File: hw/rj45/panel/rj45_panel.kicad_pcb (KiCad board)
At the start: 6 copper layers, 71.4 x 107 mm, 471 parts, among them J1 SFP edge (INF-8074i), J2 KH-RJ45-58-8P8C, T1 LP72450ANL, U1 RTL8221B-VB-CG, U2 STM32G031F6P6, U3 TPS62822DLC, U4 TPS22918DBVR, X1 MST8011AI-72-33E25

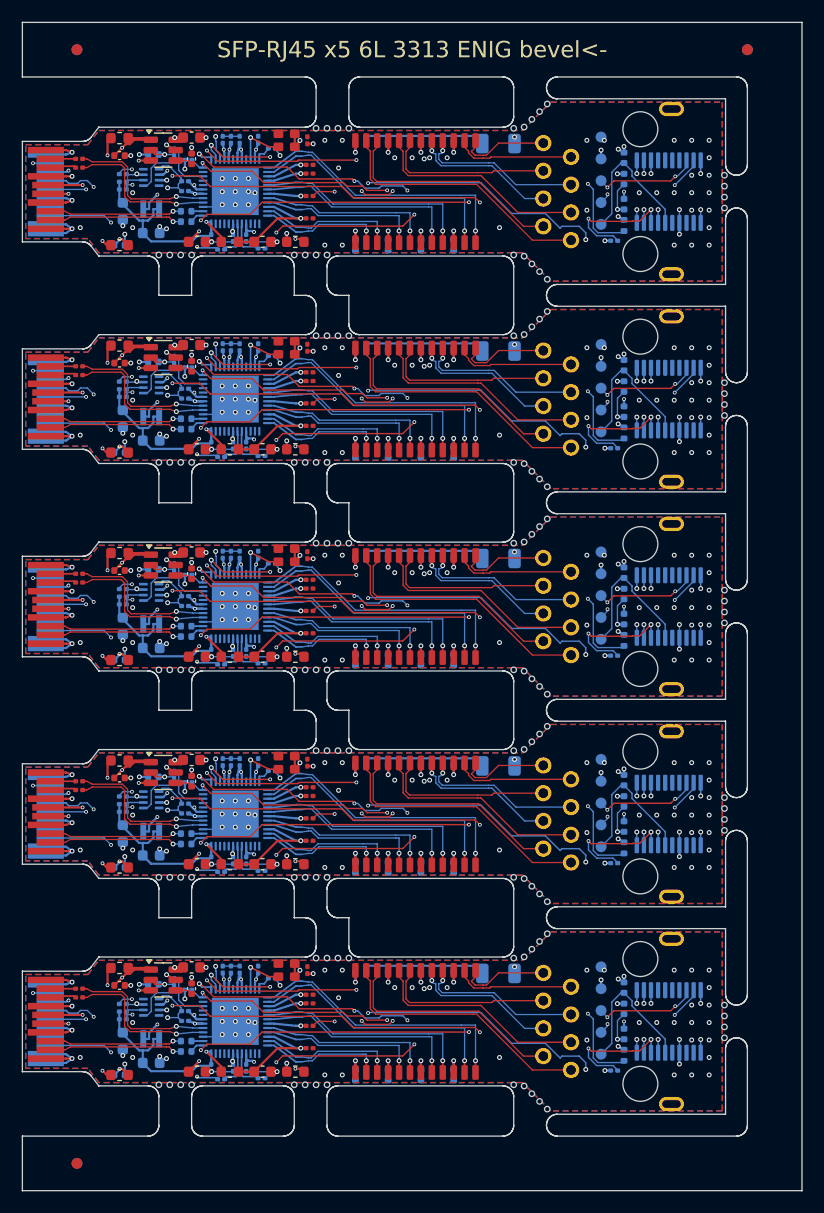
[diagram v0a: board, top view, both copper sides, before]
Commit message: RJ45 re-laid on the corrected SFP edge: U1 on top
With the edge drawn the right way round (SFF-8419 Figure 7-2) the RTL8221B's
SerDes pins meet RD-, RD+, TD+, TD- straight only from the top side; it has
no SerDes polarity swap. U1's group (decaps, straps, fan, oscillator, analog
beads, HSO caps) is turned over as one body in make_rj45.py; the links to
the rest are laid new:
- HSI and RD pairs on top, P to P, no via
- MDI on top under the magnetics' body straight into the chip-side pads,
  port 0 on channel 1; CFG_OPT1 now pulled down (no MDI swap)
- the slow lines laid on In2 end to end in the jack bus's lane order; the
  MCU's GPIOs follow it (fw VARIANT_RJ45: PA0 MDIO, PA1 MDC, PA4 TX_FAULT,
  PA5 TX_DISABLE, PA6 RX_LOS)
- both VCC beads, the load switch and its caps below the HSI pair; the
  buck's switch node under its own body; panel tabs moved off U4 and X1
DRC 0 / 0 unconnected, ERC 0, KiCad 9 PASS, panel 0 errors. T1S still
carries the mirrored edge.
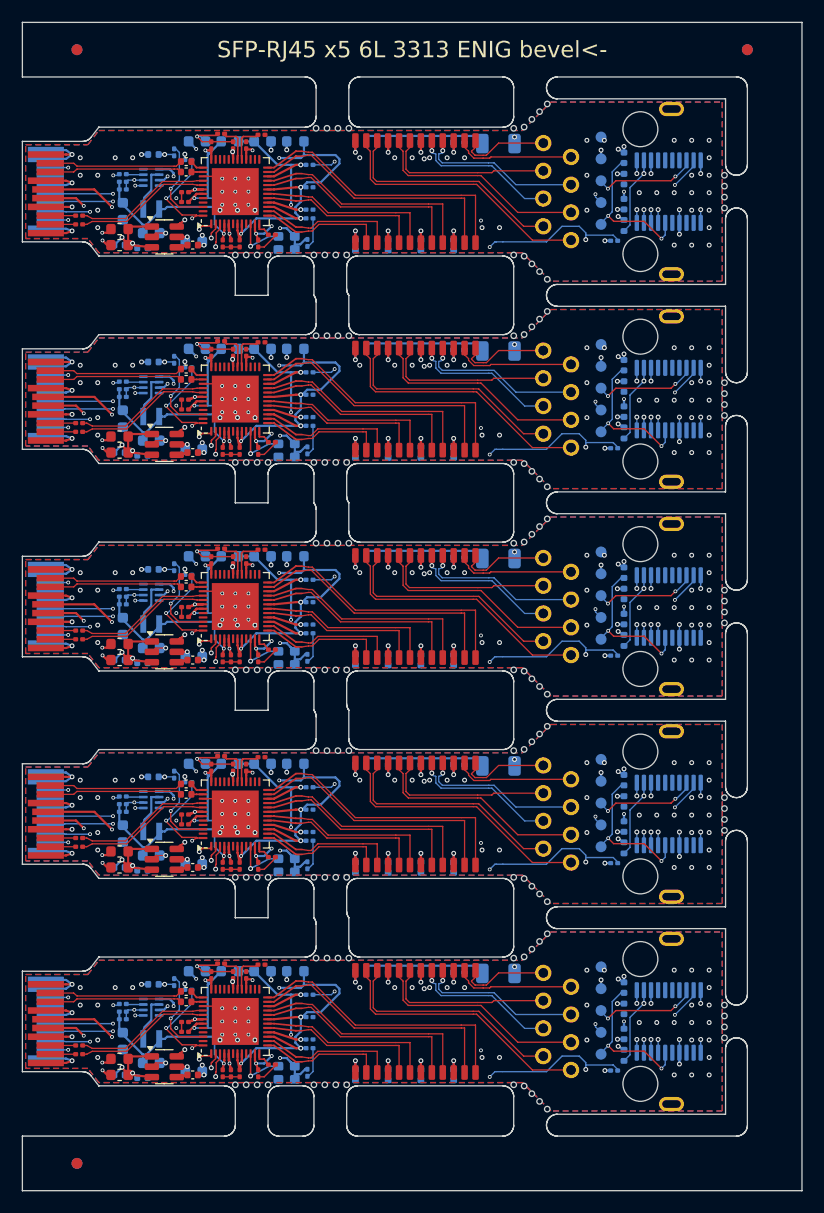
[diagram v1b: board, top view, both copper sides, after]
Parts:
- removed the C1 at (121.7, 89.2)
- removed the C1 at (121.7, 70.2)
- removed the C1 at (121.7, 51.2)
- removed the C1 at (121.7, 108.2)
- removed the C1 at (121.7, 32.2)
- removed the C10 at (134.4, 49.8)
- removed the C10 at (134.4, 87.8)
- removed the C10 at (134.4, 30.8)
- removed the C10 at (134.4, 106.8)
- removed the C10 at (134.4, 68.8)
- removed the C11 at (139.1, 109.0)
- removed the C11 at (139.1, 71.0)
- removed the C11 at (139.1, 33.0)
- removed the C11 at (139.1, 90.0)
- removed the C11 at (139.1, 52.0)
- removed the C12 at (139.1, 33.9)
- removed the C12 at (139.1, 52.9)
- removed the C12 at (139.1, 71.8)
- removed the C12 at (139.1, 90.8)
- removed the C12 at (139.1, 109.8)
- removed the C13 at (139.1, 73.9)
- removed the C13 at (139.1, 35.9)
- removed the C13 at (139.1, 54.9)
- removed the C13 at (139.1, 92.9)
- removed the C13 at (139.1, 111.9)
- removed the C14 at (139.1, 57.0)
- removed the C14 at (139.1, 95.0)
- removed the C14 at (139.1, 38.0)
- removed the C14 at (139.1, 114.0)
- removed the C14 at (139.1, 76.0)
- removed the C15 at (133.3, 77.8)
- removed the C15 at (133.3, 96.8)
- removed the C15 at (133.3, 58.8)
- removed the C15 at (133.3, 39.8)
- removed the C15 at (133.3, 115.8)
- removed the C16 at (132.1, 58.8)
- removed the C16 at (132.1, 115.8)
- removed the C16 at (132.1, 96.8)
- removed the C16 at (132.1, 39.8)
- removed the C16 at (132.1, 77.8)
- removed the C17 at (130.1, 77.8)
- removed the C17 at (130.1, 39.8)
- removed the C17 at (130.1, 58.8)
- removed the C17 at (130.1, 115.8)
- removed the C17 at (130.1, 96.8)
- removed the C18 at (127.7, 92.5)
- removed the C18 at (127.7, 73.5)
- removed the C18 at (127.7, 111.5)
- removed the C18 at (127.7, 35.5)
- removed the C18 at (127.7, 54.5)
- removed the C19 at (127.7, 34.5)
- removed the C19 at (127.7, 110.5)
- removed the C19 at (127.7, 53.5)
- removed the C19 at (127.7, 72.5)
- removed the C19 at (127.7, 91.5)
- removed the C21 at (134.8, 59.1)
- removed the C21 at (134.8, 116.1)
- removed the C21 at (134.8, 97.1)
- removed the C21 at (134.8, 78.1)
- removed the C21 at (134.8, 40.1)
- removed the C22 at (128.8, 40.1)
- removed the C22 at (128.8, 78.1)
- removed the C22 at (128.8, 97.1)
- removed the C22 at (128.8, 59.1)
- removed the C22 at (128.8, 116.1)
- removed the C3 at (118.0, 90.3)
- removed the C3 at (118.0, 33.3)
- removed the C3 at (118.0, 109.3)
- removed the C3 at (118.0, 71.3)
- removed the C3 at (118.0, 52.3)
- removed the C30 at (138.9, 106.8)
- removed the C30 at (138.9, 30.8)
- removed the C30 at (138.9, 68.8)
- removed the C30 at (138.9, 87.8)
- removed the C30 at (138.9, 49.8)
- removed the C4 at (118.0, 108.5)
- removed the C4 at (118.0, 70.5)
- removed the C4 at (118.0, 51.5)
- removed the C4 at (118.0, 89.5)
- removed the C4 at (118.0, 32.5)
- removed the C44 at (128.3, 89.5)
- removed the C44 at (128.3, 32.5)
- removed the C44 at (128.3, 108.5)
- removed the C44 at (128.3, 70.5)
- removed the C44 at (128.3, 51.5)
- removed the C45 at (128.3, 68.5)
- removed the C45 at (128.3, 87.5)
- removed the C45 at (128.3, 49.5)
- removed the C45 at (128.3, 106.5)
- removed the C45 at (128.3, 30.6)
- removed the C5 at (127.8, 56.3)
- removed the C5 at (127.8, 94.3)
- removed the C5 at (127.8, 37.3)
- removed the C5 at (127.8, 113.3)
- removed the C5 at (127.8, 75.3)
- removed the C6 at (127.8, 114.2)
- removed the C6 at (127.8, 38.2)
- removed the C6 at (127.8, 95.2)
- removed the C6 at (127.8, 76.2)
- removed the C6 at (127.8, 57.2)
- removed the C7 at (131.2, 106.8)
- removed the C7 at (131.2, 49.8)
- removed the C7 at (131.2, 30.8)
- removed the C7 at (131.2, 68.8)
- removed the C7 at (131.2, 87.8)
- removed the C8 at (131.9, 30.8)
- removed the C8 at (131.9, 106.8)
- removed the C8 at (131.9, 87.8)
- removed the C8 at (131.9, 68.8)
- removed the C8 at (131.9, 49.8)
- removed the C9 at (132.7, 87.8)
- removed the C9 at (132.7, 106.8)
- removed the C9 at (132.7, 68.8)
- removed the C9 at (132.7, 49.8)
- removed the C9 at (132.7, 30.8)
- removed the FB1 at (121.7, 49.6)
- removed the FB1 at (121.7, 87.6)
- removed the FB1 at (121.7, 30.6)
- removed the FB1 at (121.7, 68.6)
- removed the FB1 at (121.7, 106.6)
- removed the FB2 at (121.7, 78.4)
- removed the FB2 at (121.7, 116.4)
- removed the FB2 at (121.7, 40.4)
- removed the FB2 at (121.7, 59.4)
- removed the FB2 at (121.7, 97.4)
- removed the FB3 at (131.8, 97.1)
- removed the FB3 at (131.8, 116.1)
- removed the FB3 at (131.8, 59.1)
- removed the FB3 at (131.8, 40.1)
- removed the FB3 at (131.8, 78.1)
- removed the FB4 at (137.8, 116.1)
- removed the FB4 at (137.8, 97.1)
- removed the FB4 at (137.8, 78.1)
- removed the FB4 at (137.8, 40.1)
- removed the FB4 at (137.8, 59.1)
- removed KiKit_MB_12_5, KiKit_MB_18_5, KiKit_MB_24_5, KiKit_MB_30_5, KiKit_MB_6_5: NPTH, NPTH
- removed the R12 at (134.7, 116.7)
- removed the R12 at (134.7, 78.7)
- removed the R12 at (134.7, 40.7)
- removed the R12 at (134.7, 97.7)
- removed the R12 at (134.7, 59.7)
- removed the R13 at (131.0, 116.8)
- removed the R13 at (131.0, 59.8)
- removed the R13 at (131.0, 40.8)
- removed the R13 at (131.0, 78.8)
- removed the R13 at (131.0, 97.8)
- removed the R9 at (135.7, 88.5)
- removed the R9 at (135.7, 31.6)
- removed the R9 at (135.7, 107.5)
- removed the R9 at (135.7, 69.5)
- removed the R9 at (135.7, 50.5)
- removed the U4 at (125.7, 69.7)
- removed the U4 at (125.7, 50.7)
- removed the U4 at (125.7, 107.7)
- removed the U4 at (125.7, 88.7)
- removed the U4 at (125.7, 31.7)
- removed the X1 at (137.0, 30.8)
- removed the X1 at (137.0, 68.8)
- removed the X1 at (137.0, 106.8)
- removed the X1 at (137.0, 49.8)
- removed the X1 at (137.0, 87.8)
- added C1: 1uF, Capacitor_SMD:C_0402_1005Metric, B.Cu at (123.8, 116.7)
- added C1: 1uF, Capacitor_SMD:C_0402_1005Metric, B.Cu at (123.8, 78.7)
- added C1: 1uF, Capacitor_SMD:C_0402_1005Metric, B.Cu at (123.8, 97.7)
- added C1: 1uF, Capacitor_SMD:C_0402_1005Metric, B.Cu at (123.8, 59.6)
- added C1: 1uF, Capacitor_SMD:C_0402_1005Metric, B.Cu at (123.8, 40.6)
- added C10: 100nF, Capacitor_SMD:C_0201_0603Metric, F.Cu at (134.4, 59.2)
- added C10: 100nF, Capacitor_SMD:C_0201_0603Metric, F.Cu at (134.4, 116.2)
- added C10: 100nF, Capacitor_SMD:C_0201_0603Metric, F.Cu at (134.4, 40.2)
- added C10: 100nF, Capacitor_SMD:C_0201_0603Metric, F.Cu at (134.4, 97.2)
- added C10: 100nF, Capacitor_SMD:C_0201_0603Metric, F.Cu at (134.4, 78.2)
- added C11: 100nF, Capacitor_SMD:C_0201_0603Metric, B.Cu at (139.1, 57.0)
- added C11: 100nF, Capacitor_SMD:C_0201_0603Metric, B.Cu at (139.1, 38.0)
- added C11: 100nF, Capacitor_SMD:C_0201_0603Metric, B.Cu at (139.1, 95.0)
- added C11: 100nF, Capacitor_SMD:C_0201_0603Metric, B.Cu at (139.1, 114.0)
- added C11: 100nF, Capacitor_SMD:C_0201_0603Metric, B.Cu at (139.1, 76.0)
- added C12: 100nF, Capacitor_SMD:C_0201_0603Metric, B.Cu at (139.1, 56.1)
- added C12: 100nF, Capacitor_SMD:C_0201_0603Metric, B.Cu at (139.1, 94.2)
- added C12: 100nF, Capacitor_SMD:C_0201_0603Metric, B.Cu at (139.1, 37.1)
- added C12: 100nF, Capacitor_SMD:C_0201_0603Metric, B.Cu at (139.1, 113.2)
- added C12: 100nF, Capacitor_SMD:C_0201_0603Metric, B.Cu at (139.1, 75.2)
- added C13: 100nF, Capacitor_SMD:C_0201_0603Metric, B.Cu at (139.1, 35.1)
- added C13: 100nF, Capacitor_SMD:C_0201_0603Metric, B.Cu at (139.1, 111.1)
- added C13: 100nF, Capacitor_SMD:C_0201_0603Metric, B.Cu at (139.1, 73.1)
- added C13: 100nF, Capacitor_SMD:C_0201_0603Metric, B.Cu at (139.1, 54.1)
- added C13: 100nF, Capacitor_SMD:C_0201_0603Metric, B.Cu at (139.1, 92.1)
- added C14: 100nF, Capacitor_SMD:C_0201_0603Metric, B.Cu at (139.1, 52.0)
- added C14: 100nF, Capacitor_SMD:C_0201_0603Metric, B.Cu at (139.1, 90.0)
- added C14: 100nF, Capacitor_SMD:C_0201_0603Metric, B.Cu at (139.1, 33.0)
- added C14: 100nF, Capacitor_SMD:C_0201_0603Metric, B.Cu at (139.1, 109.0)
- added C14: 100nF, Capacitor_SMD:C_0201_0603Metric, B.Cu at (139.1, 71.0)
- added C15: 100nF, Capacitor_SMD:C_0201_0603Metric, F.Cu at (133.3, 107.2)
- added C15: 100nF, Capacitor_SMD:C_0201_0603Metric, F.Cu at (133.3, 50.2)
- added C15: 100nF, Capacitor_SMD:C_0201_0603Metric, F.Cu at (133.3, 31.2)
- added C15: 100nF, Capacitor_SMD:C_0201_0603Metric, F.Cu at (133.3, 69.2)
- added C15: 100nF, Capacitor_SMD:C_0201_0603Metric, F.Cu at (133.3, 88.2)
- added C16: 100nF, Capacitor_SMD:C_0201_0603Metric, F.Cu at (132.1, 88.2)
- added C16: 100nF, Capacitor_SMD:C_0201_0603Metric, F.Cu at (132.1, 50.2)
- added C16: 100nF, Capacitor_SMD:C_0201_0603Metric, F.Cu at (132.1, 107.2)
- added C16: 100nF, Capacitor_SMD:C_0201_0603Metric, F.Cu at (132.1, 69.2)
- added C16: 100nF, Capacitor_SMD:C_0201_0603Metric, F.Cu at (132.1, 31.2)
- added C17: 100nF, Capacitor_SMD:C_0201_0603Metric, F.Cu at (130.1, 88.2)
- added C17: 100nF, Capacitor_SMD:C_0201_0603Metric, F.Cu at (130.1, 69.2)
- added C17: 100nF, Capacitor_SMD:C_0201_0603Metric, F.Cu at (130.1, 50.2)
- added C17: 100nF, Capacitor_SMD:C_0201_0603Metric, F.Cu at (130.1, 107.2)
- added C17: 100nF, Capacitor_SMD:C_0201_0603Metric, F.Cu at (130.1, 31.2)
- added C18: 100nF, Capacitor_SMD:C_0201_0603Metric, F.Cu at (127.7, 111.5)
- added C18: 100nF, Capacitor_SMD:C_0201_0603Metric, F.Cu at (127.7, 92.5)
- added C18: 100nF, Capacitor_SMD:C_0201_0603Metric, F.Cu at (127.7, 73.5)
- added C18: 100nF, Capacitor_SMD:C_0201_0603Metric, F.Cu at (127.7, 35.5)
- added C18: 100nF, Capacitor_SMD:C_0201_0603Metric, F.Cu at (127.7, 54.5)
- added C19: 100nF, Capacitor_SMD:C_0201_0603Metric, F.Cu at (127.7, 93.5)
- added C19: 100nF, Capacitor_SMD:C_0201_0603Metric, F.Cu at (127.7, 74.5)
- added C19: 100nF, Capacitor_SMD:C_0201_0603Metric, F.Cu at (127.7, 36.5)
- added C19: 100nF, Capacitor_SMD:C_0201_0603Metric, F.Cu at (127.7, 112.5)
- added C19: 100nF, Capacitor_SMD:C_0201_0603Metric, F.Cu at (127.7, 55.5)
- added C21: 10uF, Capacitor_SMD:C_0603_1608Metric, B.Cu at (134.8, 106.9)
- added C21: 10uF, Capacitor_SMD:C_0603_1608Metric, B.Cu at (134.8, 68.9)
- added C21: 10uF, Capacitor_SMD:C_0603_1608Metric, B.Cu at (134.8, 49.9)
- added C21: 10uF, Capacitor_SMD:C_0603_1608Metric, B.Cu at (134.8, 30.9)
- added C21: 10uF, Capacitor_SMD:C_0603_1608Metric, B.Cu at (134.8, 87.9)
- added C22: 10uF, Capacitor_SMD:C_0603_1608Metric, B.Cu at (128.8, 106.9)
- added C22: 10uF, Capacitor_SMD:C_0603_1608Metric, B.Cu at (128.8, 68.9)
- added C22: 10uF, Capacitor_SMD:C_0603_1608Metric, B.Cu at (128.8, 49.9)
- added C22: 10uF, Capacitor_SMD:C_0603_1608Metric, B.Cu at (128.8, 87.9)
- added C22: 10uF, Capacitor_SMD:C_0603_1608Metric, B.Cu at (128.8, 30.9)
- added C3: 100nF, Capacitor_SMD:C_0201_0603Metric, F.Cu at (118.0, 75.7)
- added C3: 100nF, Capacitor_SMD:C_0201_0603Metric, F.Cu at (118.0, 56.7)
- added C3: 100nF, Capacitor_SMD:C_0201_0603Metric, F.Cu at (118.0, 37.7)
- added C3: 100nF, Capacitor_SMD:C_0201_0603Metric, F.Cu at (118.0, 113.7)
- added C3: 100nF, Capacitor_SMD:C_0201_0603Metric, F.Cu at (118.0, 94.7)
- added C30: 100nF, Capacitor_SMD:C_0201_0603Metric, B.Cu at (138.9, 78.2)
- added C30: 100nF, Capacitor_SMD:C_0201_0603Metric, B.Cu at (138.9, 116.2)
- added C30: 100nF, Capacitor_SMD:C_0201_0603Metric, B.Cu at (138.9, 40.2)
- added C30: 100nF, Capacitor_SMD:C_0201_0603Metric, B.Cu at (138.9, 97.2)
- added C30: 100nF, Capacitor_SMD:C_0201_0603Metric, B.Cu at (138.9, 59.2)
- added C4: 100nF, Capacitor_SMD:C_0201_0603Metric, F.Cu at (118.0, 95.5)
- added C4: 100nF, Capacitor_SMD:C_0201_0603Metric, F.Cu at (118.0, 76.5)
- added C4: 100nF, Capacitor_SMD:C_0201_0603Metric, F.Cu at (118.0, 38.5)
- added C4: 100nF, Capacitor_SMD:C_0201_0603Metric, F.Cu at (118.0, 57.5)
- added C4: 100nF, Capacitor_SMD:C_0201_0603Metric, F.Cu at (118.0, 114.5)
- added C44: 2.2nF, Capacitor_SMD:C_0402_1005Metric, F.Cu at (128.4, 40.4)
- added C44: 2.2nF, Capacitor_SMD:C_0402_1005Metric, F.Cu at (128.4, 116.4)
- added C44: 2.2nF, Capacitor_SMD:C_0402_1005Metric, F.Cu at (128.4, 78.4)
- added C44: 2.2nF, Capacitor_SMD:C_0402_1005Metric, F.Cu at (128.4, 59.4)
- added C44: 2.2nF, Capacitor_SMD:C_0402_1005Metric, F.Cu at (128.4, 97.4)
- added C45: 10uF, Capacitor_SMD:C_0603_1608Metric, B.Cu at (128.5, 116.1)
- added C45: 10uF, Capacitor_SMD:C_0603_1608Metric, B.Cu at (128.5, 40.1)
- added C45: 10uF, Capacitor_SMD:C_0603_1608Metric, B.Cu at (128.5, 97.1)
- added C45: 10uF, Capacitor_SMD:C_0603_1608Metric, B.Cu at (128.5, 78.1)
- added C45: 10uF, Capacitor_SMD:C_0603_1608Metric, B.Cu at (128.5, 59.1)
- added C5: 100nF, Capacitor_SMD:C_0402_1005Metric, F.Cu at (127.8, 33.7)
- added C5: 100nF, Capacitor_SMD:C_0402_1005Metric, F.Cu at (127.8, 90.7)
- added C5: 100nF, Capacitor_SMD:C_0402_1005Metric, F.Cu at (127.8, 52.7)
- added C5: 100nF, Capacitor_SMD:C_0402_1005Metric, F.Cu at (127.8, 109.7)
- added C5: 100nF, Capacitor_SMD:C_0402_1005Metric, F.Cu at (127.8, 71.7)
- added C6: 100nF, Capacitor_SMD:C_0402_1005Metric, F.Cu at (127.8, 108.8)
- added C6: 100nF, Capacitor_SMD:C_0402_1005Metric, F.Cu at (127.8, 51.8)
- added C6: 100nF, Capacitor_SMD:C_0402_1005Metric, F.Cu at (127.8, 70.8)
- added C6: 100nF, Capacitor_SMD:C_0402_1005Metric, F.Cu at (127.8, 32.8)
- added C6: 100nF, Capacitor_SMD:C_0402_1005Metric, F.Cu at (127.8, 89.8)
- added C7: 100nF, Capacitor_SMD:C_0201_0603Metric, F.Cu at (131.2, 97.2)
- added C7: 100nF, Capacitor_SMD:C_0201_0603Metric, F.Cu at (131.2, 59.2)
- added C7: 100nF, Capacitor_SMD:C_0201_0603Metric, F.Cu at (131.2, 116.2)
- added C7: 100nF, Capacitor_SMD:C_0201_0603Metric, F.Cu at (131.2, 40.2)
- added C7: 100nF, Capacitor_SMD:C_0201_0603Metric, F.Cu at (131.2, 78.2)
- added C8: 100nF, Capacitor_SMD:C_0201_0603Metric, F.Cu at (131.9, 116.2)
- added C8: 100nF, Capacitor_SMD:C_0201_0603Metric, F.Cu at (131.9, 59.2)
- added C8: 100nF, Capacitor_SMD:C_0201_0603Metric, F.Cu at (131.9, 40.2)
- added C8: 100nF, Capacitor_SMD:C_0201_0603Metric, F.Cu at (131.9, 97.2)
- added C8: 100nF, Capacitor_SMD:C_0201_0603Metric, F.Cu at (131.9, 78.2)
- added C9: 100nF, Capacitor_SMD:C_0201_0603Metric, F.Cu at (132.7, 59.2)
- added C9: 100nF, Capacitor_SMD:C_0201_0603Metric, F.Cu at (132.7, 78.2)
- added C9: 100nF, Capacitor_SMD:C_0201_0603Metric, F.Cu at (132.7, 116.2)
- added C9: 100nF, Capacitor_SMD:C_0201_0603Metric, F.Cu at (132.7, 97.2)
- added C9: 100nF, Capacitor_SMD:C_0201_0603Metric, F.Cu at (132.7, 40.2)
- added FB1: BLM18KG601SH1, Inductor_SMD:L_0603_1608Metric, F.Cu at (121.7, 59.4)
- added FB1: BLM18KG601SH1, Inductor_SMD:L_0603_1608Metric, F.Cu at (121.7, 97.4)
- added FB1: BLM18KG601SH1, Inductor_SMD:L_0603_1608Metric, F.Cu at (121.7, 116.4)
- added FB1: BLM18KG601SH1, Inductor_SMD:L_0603_1608Metric, F.Cu at (121.7, 78.4)
- added FB1: BLM18KG601SH1, Inductor_SMD:L_0603_1608Metric, F.Cu at (121.7, 40.4)
- added FB2: BLM18KG601SH1, Inductor_SMD:L_0603_1608Metric, F.Cu at (121.7, 114.9)
- added FB2: BLM18KG601SH1, Inductor_SMD:L_0603_1608Metric, F.Cu at (121.7, 57.9)
- added FB2: BLM18KG601SH1, Inductor_SMD:L_0603_1608Metric, F.Cu at (121.7, 38.9)
- added FB2: BLM18KG601SH1, Inductor_SMD:L_0603_1608Metric, F.Cu at (121.7, 95.9)
- added FB2: BLM18KG601SH1, Inductor_SMD:L_0603_1608Metric, F.Cu at (121.7, 76.9)
- added FB3: BLM18KG601SH1, Inductor_SMD:L_0603_1608Metric, B.Cu at (131.8, 106.9)
- added FB3: BLM18KG601SH1, Inductor_SMD:L_0603_1608Metric, B.Cu at (131.8, 30.9)
- added FB3: BLM18KG601SH1, Inductor_SMD:L_0603_1608Metric, B.Cu at (131.8, 49.9)
- added FB3: BLM18KG601SH1, Inductor_SMD:L_0603_1608Metric, B.Cu at (131.8, 68.9)
- added FB3: BLM18KG601SH1, Inductor_SMD:L_0603_1608Metric, B.Cu at (131.8, 87.9)
- added FB4: BLM18KG601SH1, Inductor_SMD:L_0603_1608Metric, B.Cu at (137.8, 87.9)
- added FB4: BLM18KG601SH1, Inductor_SMD:L_0603_1608Metric, B.Cu at (137.8, 68.9)
- added FB4: BLM18KG601SH1, Inductor_SMD:L_0603_1608Metric, B.Cu at (137.8, 49.9)
- added FB4: BLM18KG601SH1, Inductor_SMD:L_0603_1608Metric, B.Cu at (137.8, 30.9)
- added FB4: BLM18KG601SH1, Inductor_SMD:L_0603_1608Metric, B.Cu at (137.8, 106.9)
- added KiKit_MB_10_5: NPTH, NPTH, F.Cu at (160.9, 46.5)
- added KiKit_MB_16_5: NPTH, NPTH, F.Cu at (160.9, 65.5)
- added KiKit_MB_22_5: NPTH, NPTH, F.Cu at (160.9, 84.5)
- added KiKit_MB_28_5: NPTH, NPTH, F.Cu at (160.9, 103.5)
- added KiKit_MB_4_5: NPTH, NPTH, F.Cu at (160.9, 27.5)
- added R12: 4.7k, Resistor_SMD:R_0201_0603Metric, F.Cu at (134.7, 30.3)
- added R12: 4.7k, Resistor_SMD:R_0201_0603Metric, F.Cu at (134.7, 106.3)
- added R12: 4.7k, Resistor_SMD:R_0201_0603Metric, F.Cu at (134.7, 87.3)
- added R12: 4.7k, Resistor_SMD:R_0201_0603Metric, F.Cu at (134.7, 68.3)
- added R12: 4.7k, Resistor_SMD:R_0201_0603Metric, F.Cu at (134.7, 49.3)
- added R13: 4.7k, Resistor_SMD:R_0201_0603Metric, F.Cu at (131.0, 30.2)
- added R13: 4.7k, Resistor_SMD:R_0201_0603Metric, F.Cu at (131.0, 87.2)
- added R13: 4.7k, Resistor_SMD:R_0201_0603Metric, F.Cu at (131.0, 49.2)
- added R13: 4.7k, Resistor_SMD:R_0201_0603Metric, F.Cu at (131.0, 68.2)
- added R13: 4.7k, Resistor_SMD:R_0201_0603Metric, F.Cu at (131.0, 106.2)
- added R9: 2.49k 1%, Resistor_SMD:R_0201_0603Metric, F.Cu at (135.7, 77.5)
- added R9: 2.49k 1%, Resistor_SMD:R_0201_0603Metric, F.Cu at (135.7, 58.5)
- added R9: 2.49k 1%, Resistor_SMD:R_0201_0603Metric, F.Cu at (135.7, 115.5)
- added R9: 2.49k 1%, Resistor_SMD:R_0201_0603Metric, F.Cu at (135.7, 39.5)
- added R9: 2.49k 1%, Resistor_SMD:R_0201_0603Metric, F.Cu at (135.7, 96.5)
- added U4: TPS22918DBVR, Package_TO_SOT_SMD:SOT-23-6, F.Cu at (125.8, 39.6)
- added U4: TPS22918DBVR, Package_TO_SOT_SMD:SOT-23-6, F.Cu at (125.8, 96.7)
- added U4: TPS22918DBVR, Package_TO_SOT_SMD:SOT-23-6, F.Cu at (125.8, 77.7)
- added U4: TPS22918DBVR, Package_TO_SOT_SMD:SOT-23-6, F.Cu at (125.8, 115.7)
- added U4: TPS22918DBVR, Package_TO_SOT_SMD:SOT-23-6, F.Cu at (125.8, 58.6)
- added X1: MST8011AI-72-33E25, sfp:Oscillator_SMD_MST_2016-4Pin, B.Cu at (137.0, 116.2)
- added X1: MST8011AI-72-33E25, sfp:Oscillator_SMD_MST_2016-4Pin, B.Cu at (137.0, 40.2)
- added X1: MST8011AI-72-33E25, sfp:Oscillator_SMD_MST_2016-4Pin, B.Cu at (137.0, 78.2)
- added X1: MST8011AI-72-33E25, sfp:Oscillator_SMD_MST_2016-4Pin, B.Cu at (137.0, 59.2)
- added X1: MST8011AI-72-33E25, sfp:Oscillator_SMD_MST_2016-4Pin, B.Cu at (137.0, 97.2)
- U1 (x5): moved to F.Cu
- moved KiKit_MB_13_4 52.0 mm to (177.1, 75.0)
- moved KiKit_MB_19_4 52.0 mm to (177.1, 94.0)
- moved KiKit_MB_1_4 52.0 mm to (177.1, 37.0)
- moved KiKit_MB_25_4 52.0 mm to (177.1, 113.0)
- moved KiKit_MB_7_4 52.0 mm to (177.1, 56.0)
- moved KiKit_MB_13_3 51.1 mm to (177.1, 74.0)
- moved KiKit_MB_19_3 51.1 mm to (177.1, 93.0)
- moved KiKit_MB_1_3 51.1 mm to (177.1, 36.0)
- moved KiKit_MB_25_3 51.1 mm to (177.1, 112.0)
- moved KiKit_MB_7_3 51.1 mm to (177.1, 55.0)
- moved KiKit_MB_13_2 50.2 mm to (177.1, 73.0)
- moved KiKit_MB_19_2 50.2 mm to (177.1, 92.0)
- moved KiKit_MB_1_2 50.2 mm to (177.1, 35.0)
- moved KiKit_MB_25_2 50.2 mm to (177.1, 111.0)
- moved KiKit_MB_7_2 50.2 mm to (177.1, 54.0)
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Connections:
- T1 pad 11: Board_1-MDI0_N -> Board_1-MDI3_P
- T1 pad 12: Board_1-MDI0_P -> Board_1-MDI3_N
- T1 pad 2: Board_1-MDI3_N -> Board_1-MDI0_P
- T1 pad 3: Board_1-MDI3_P -> Board_1-MDI0_N
- T1 pad 5: Board_1-MDI2_N -> Board_1-MDI1_P
- T1 pad 6: Board_1-MDI2_P -> Board_1-MDI1_N
- T1 pad 8: Board_1-MDI1_N -> Board_1-MDI2_P
- T1 pad 9: Board_1-MDI1_P -> Board_1-MDI2_N
- T1 pad 11: Board_4-MDI0_N -> Board_4-MDI3_P
- T1 pad 12: Board_4-MDI0_P -> Board_4-MDI3_N
- T1 pad 2: Board_4-MDI3_N -> Board_4-MDI0_P
- T1 pad 3: Board_4-MDI3_P -> Board_4-MDI0_N
- T1 pad 5: Board_4-MDI2_N -> Board_4-MDI1_P
- T1 pad 6: Board_4-MDI2_P -> Board_4-MDI1_N
- T1 pad 8: Board_4-MDI1_N -> Board_4-MDI2_P
- T1 pad 9: Board_4-MDI1_P -> Board_4-MDI2_N
- T1 pad 11: Board_0-MDI0_N -> Board_0-MDI3_P
- T1 pad 12: Board_0-MDI0_P -> Board_0-MDI3_N
- T1 pad 2: Board_0-MDI3_N -> Board_0-MDI0_P
- T1 pad 3: Board_0-MDI3_P -> Board_0-MDI0_N
- T1 pad 5: Board_0-MDI2_N -> Board_0-MDI1_P
- T1 pad 6: Board_0-MDI2_P -> Board_0-MDI1_N
- T1 pad 8: Board_0-MDI1_N -> Board_0-MDI2_P
- T1 pad 9: Board_0-MDI1_P -> Board_0-MDI2_N
- T1 pad 11: Board_3-MDI0_N -> Board_3-MDI3_P
- T1 pad 12: Board_3-MDI0_P -> Board_3-MDI3_N
- T1 pad 2: Board_3-MDI3_N -> Board_3-MDI0_P
- T1 pad 3: Board_3-MDI3_P -> Board_3-MDI0_N
- T1 pad 5: Board_3-MDI2_N -> Board_3-MDI1_P
- T1 pad 6: Board_3-MDI2_P -> Board_3-MDI1_N
- T1 pad 8: Board_3-MDI1_N -> Board_3-MDI2_P
- T1 pad 9: Board_3-MDI1_P -> Board_3-MDI2_N
- T1 pad 11: Board_2-MDI0_N -> Board_2-MDI3_P
- T1 pad 12: Board_2-MDI0_P -> Board_2-MDI3_N
- T1 pad 2: Board_2-MDI3_N -> Board_2-MDI0_P
- T1 pad 3: Board_2-MDI3_P -> Board_2-MDI0_N
- T1 pad 5: Board_2-MDI2_N -> Board_2-MDI1_P
- T1 pad 6: Board_2-MDI2_P -> Board_2-MDI1_N
- T1 pad 8: Board_2-MDI1_N -> Board_2-MDI2_P
- T1 pad 9: Board_2-MDI1_P -> Board_2-MDI2_N
- U2 pad 11: Board_3-TX_DISABLE -> Board_3-TX_FAULT
- U2 pad 12: Board_3-RX_LOS -> Board_3-TX_DISABLE
- U2 pad 13: Board_3-TX_FAULT -> Board_3-RX_LOS
- U2 pad 7: Board_3-MDC -> Board_3-MDIO
- U2 pad 8: Board_3-MDIO -> Board_3-MDC
- U2 pad 11: Board_2-TX_DISABLE -> Board_2-TX_FAULT
- U2 pad 12: Board_2-RX_LOS -> Board_2-TX_DISABLE
- U2 pad 13: Board_2-TX_FAULT -> Board_2-RX_LOS
- U2 pad 7: Board_2-MDC -> Board_2-MDIO
- U2 pad 8: Board_2-MDIO -> Board_2-MDC
- U2 pad 11: Board_4-TX_DISABLE -> Board_4-TX_FAULT
- U2 pad 12: Board_4-RX_LOS -> Board_4-TX_DISABLE
- U2 pad 13: Board_4-TX_FAULT -> Board_4-RX_LOS
- U2 pad 7: Board_4-MDC -> Board_4-MDIO
- U2 pad 8: Board_4-MDIO -> Board_4-MDC
- U2 pad 11: Board_1-TX_DISABLE -> Board_1-TX_FAULT
- U2 pad 12: Board_1-RX_LOS -> Board_1-TX_DISABLE
- U2 pad 13: Board_1-TX_FAULT -> Board_1-RX_LOS
- U2 pad 7: Board_1-MDC -> Board_1-MDIO
- U2 pad 8: Board_1-MDIO -> Board_1-MDC
- U2 pad 11: Board_0-TX_DISABLE -> Board_0-TX_FAULT
- U2 pad 12: Board_0-RX_LOS -> Board_0-TX_DISABLE
- U2 pad 13: Board_0-TX_FAULT -> Board_0-RX_LOS
- U2 pad 7: Board_0-MDC -> Board_0-MDIO
- U2 pad 8: Board_0-MDIO -> Board_0-MDC
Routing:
- net Board_0-+3V3: track 23.8 -> 43.7 mm, vias 19 -> 18
- net Board_1-+3V3: track 23.8 -> 43.7 mm, vias 19 -> 18
- net Board_3-+3V3: track 23.8 -> 43.7 mm, vias 19 -> 18
- net Board_2-+3V3: track 23.8 -> 43.7 mm, vias 19 -> 18
- net Board_4-+3V3: track 23.8 -> 43.7 mm, vias 19 -> 18
- net Board_1-MDI3_N: track 11.5 -> 25.5 mm, vias 1 -> 0
- net Board_1-MDI0_P: track 25.5 -> 11.5 mm, vias 1 -> 0
- net Board_0-MDI3_N: track 11.5 -> 25.5 mm, vias 1 -> 0
- net Board_0-MDI0_P: track 25.5 -> 11.5 mm, vias 1 -> 0
- net Board_4-MDI3_N: track 11.5 -> 25.5 mm, vias 1 -> 0
- net Board_4-MDI0_P: track 25.5 -> 11.5 mm, vias 1 -> 0
- net Board_3-MDI3_N: track 11.5 -> 25.5 mm, vias 1 -> 0
- net Board_3-MDI0_P: track 25.5 -> 11.5 mm, vias 1 -> 0
- net Board_2-MDI3_N: track 11.5 -> 25.5 mm, vias 1 -> 0
- net Board_2-MDI0_P: track 25.5 -> 11.5 mm, vias 1 -> 0
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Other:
- outline, holes or cut-outs redrawn
